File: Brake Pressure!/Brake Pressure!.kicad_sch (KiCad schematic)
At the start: 12 parts, among them J1 DTF13-6P, Q1 Q_Photo_NPN_EBC, U3 MCP2515-I, U4 TJA1050DRG, X1 ${ALTIUM_VALUE}

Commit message: Update Brake Pressure!.kicad_sch
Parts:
- renumbered C11 to C1, C12 to C2, C13 to C3, C14 to C4, C15 to C5, R13 to R3
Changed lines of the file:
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@@
 		(on_board yes)
 		(dnp no)
-		(property "Reference" "C14"
+		(property "Reference" "C4"
 			(at 96.901 144.272 0)
 			(effects
@@
 			(project "Brake Pressure!"
 				(path "/966ccee8-1e79-48cc-adf9-5a781a378016"
-					(reference "C14")
+					(reference "C4")
 					(unit 0)
 				)
@@
 		(on_board yes)
 		(dnp no)
-		(property "Reference" "C13"
+		(property "Reference" "C3"
 			(at 96.139 134.112 0)
 			(effects
@@
 			(project "Brake Pressure!"
 				(path "/966ccee8-1e79-48cc-adf9-5a781a378016"
-					(reference "C13")
+					(reference "C3")
 					(unit 0)
 				)
@@
 		(on_board yes)
 		(dnp no)
-		(property "Reference" "C11"
+		(property "Reference" "C1"
 			(at 61.722 127.762 0)
 			(effects
@@
 			(project "Brake Pressure!"
 				(path "/966ccee8-1e79-48cc-adf9-5a781a378016"
-					(reference "C11")
+					(reference "C1")
 					(unit 0)
 				)
@@
 		(on_board yes)
 		(dnp no)
-		(property "Reference" "C12"
+		(property "Reference" "C2"
 			(at 90.17 127 0)
 			(effects
@@
 			(project "Brake Pressure!"
 				(path "/966ccee8-1e79-48cc-adf9-5a781a378016"
-					(reference "C12")
+					(reference "C2")
 					(unit 0)
 				)
@@
 		(on_board yes)
 		(dnp no)
-		(property "Reference" "C15"
+		(property "Reference" "C5"
 			(at 246.38 135.89 0)
 			(effects
@@
 			(project "Brake Pressure!"
 				(path "/966ccee8-1e79-48cc-adf9-5a781a378016"
-					(reference "C15")
+					(reference "C5")
 					(unit 0)
 				)
@@
 		(dnp no)
 		(fields_autoplaced yes)
-		(property "Reference" "R13"
+		(property "Reference" "R3"
 			(at 109.22 115.57 90)
 			(effects
@@
 			(project "Brake Pressure!"
 				(path "/966ccee8-1e79-48cc-adf9-5a781a378016"
-					(reference "R13")
+					(reference "R3")
 					(unit 1)
 				)

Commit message: brake pressure
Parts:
- renumbered U4 to U1, U3 to U2
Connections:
- no-connect marks 8 -> 7
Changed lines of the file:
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@@
-	)
-	(no_connect
-		(at 156.21 129.54)
 	)
 	(no_connect
@@
 	(wire
 		(pts
+			(xy 25.4 38.1) (xy 30.48 38.1)
+		)
+		(stroke
+			(width 0)
+			(type default)
+		)
+	)
+	(wire
+		(pts
 			(xy 177.8 111.76) (xy 177.8 121.92)
 		)
@@
 	(wire
 		(pts
+			(xy 25.4 165.1) (xy 25.4 38.1)
+		)
+		(stroke
+			(width 0)
+			(type default)
+		)
+	)
+	(wire
+		(pts
 			(xy 104.14 133.35) (xy 104.14 134.62)
 		)
@@
 	(wire
 		(pts
+			(xy 163.83 165.1) (xy 25.4 165.1)
+		)
+		(stroke
+			(width 0)
+			(type default)
+		)
+	)
+	(wire
+		(pts
 			(xy 236.22 121.92) (xy 257.81 121.92)
 		)
@@
 	(wire
 		(pts
+			(xy 156.21 129.54) (xy 163.83 129.54)
+		)
+		(stroke
+			(width 0)
+			(type default)
+		)
+	)
+	(wire
+		(pts
 			(xy 43.18 81.28) (xy 43.18 85.09)
 		)
@@
 		(pts
 			(xy 93.98 113.03) (xy 93.98 121.92)
+		)
+		(stroke
+			(width 0)
+			(type default)
+		)
+	)
+	(wire
+		(pts
+			(xy 163.83 129.54) (xy 163.83 165.1)
 		)
 		(stroke
@@
 		(on_board yes)
 		(dnp no)
-		(property "Reference" "U4"
+		(property "Reference" "U1"
 			(at 214.63 116.84 0)
 			(effects
@@
 			(project "Brake Pressure!"
 				(path "/966ccee8-1e79-48cc-adf9-5a781a378016"
-					(reference "U4")
+					(reference "U1")
 					(unit 0)
 				)
@@
 		(on_board yes)
 		(dnp no)
-		(property "Reference" "U3"
+		(property "Reference" "U2"
 			(at 123.19 104.14 0)
 			(effects
@@
 			(project "Brake Pressure!"
 				(path "/966ccee8-1e79-48cc-adf9-5a781a378016"
-					(reference "U3")
+					(reference "U2")
 					(unit 0)
 				)

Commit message: make new connection
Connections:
- net CS: now also A1.13 (D10)
- net SCK: now also A1.16 (SCK)
- net SI: now also A1.14 (MOSI)
- net SO: now also A1.15 (MISO)
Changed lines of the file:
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@@
+		)
+	)
+	(global_label "SCK"
+		(shape input)
+		(at 30.48 68.58 180)
+		(fields_autoplaced yes)
+		(effects
+			(font
+				(size 1.27 1.27)
+			)
+			(justify right)
+		)
+		(property "Intersheetrefs" "${INTERSHEET_REFS}"
+			(at 23.7453 68.58 0)
+			(effects
+				(font
+					(size 1.27 1.27)
+				)
+				(justify right)
+				(hide yes)
+			)
 		)
 	)
@@
 		)
 	)
+	(global_label "CS"
+		(shape input)
+		(at 30.48 58.42 180)
+		(fields_autoplaced yes)
+		(effects
+			(font
+				(size 1.27 1.27)
+			)
+			(justify right)
+		)
+		(property "Intersheetrefs" "${INTERSHEET_REFS}"
+			(at 25.0153 58.42 0)
+			(effects
+				(font
+					(size 1.27 1.27)
+				)
+				(justify right)
+				(hide yes)
+			)
+		)
+	)
 	(global_label "Low"
 		(shape input)
@@
 		)
 	)
+	(global_label "SI"
+		(shape input)
+		(at 30.48 63.5 180)
+		(fields_autoplaced yes)
+		(effects
+			(font
+				(size 1.27 1.27)
+			)
+			(justify right)
+		)
+		(property "Intersheetrefs" "${INTERSHEET_REFS}"
+			(at 25.6805 63.5 0)
+			(effects
+				(font
+					(size 1.27 1.27)
+				)
+				(justify right)
+				(hide yes)
+			)
+		)
+	)
 	(global_label "SO"
 		(shape input)
@@
 				(hide yes)
 			)
+		)
+	)
+	(global_label "SO"
+		(shape input)
+		(at 30.48 66.04 180)
+		(fields_autoplaced yes)
+		(effects
+			(font
+				(size 1.27 1.27)
+			)
+			(justify right)
+		)
+		(property "Intersheetrefs" "${INTERSHEET_REFS}"
+			(at 24.9548 66.04 0)
+			(effects
+				(font
+					(size 1.27 1.27)
+				)
+				(justify right)
+				(hide yes)
+			)

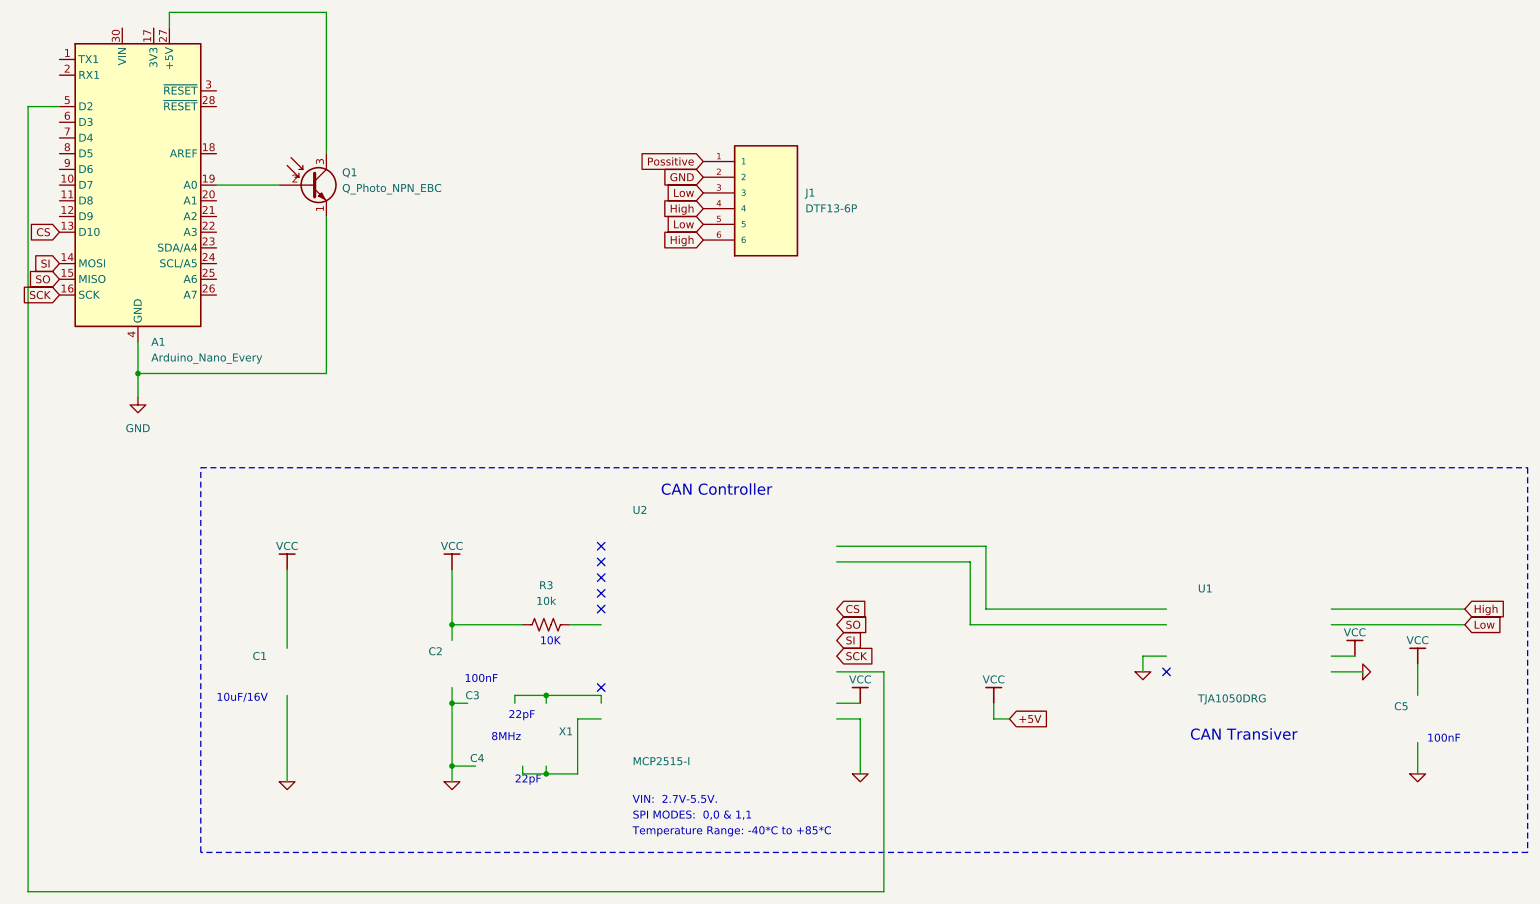
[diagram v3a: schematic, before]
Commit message: brake pressure done
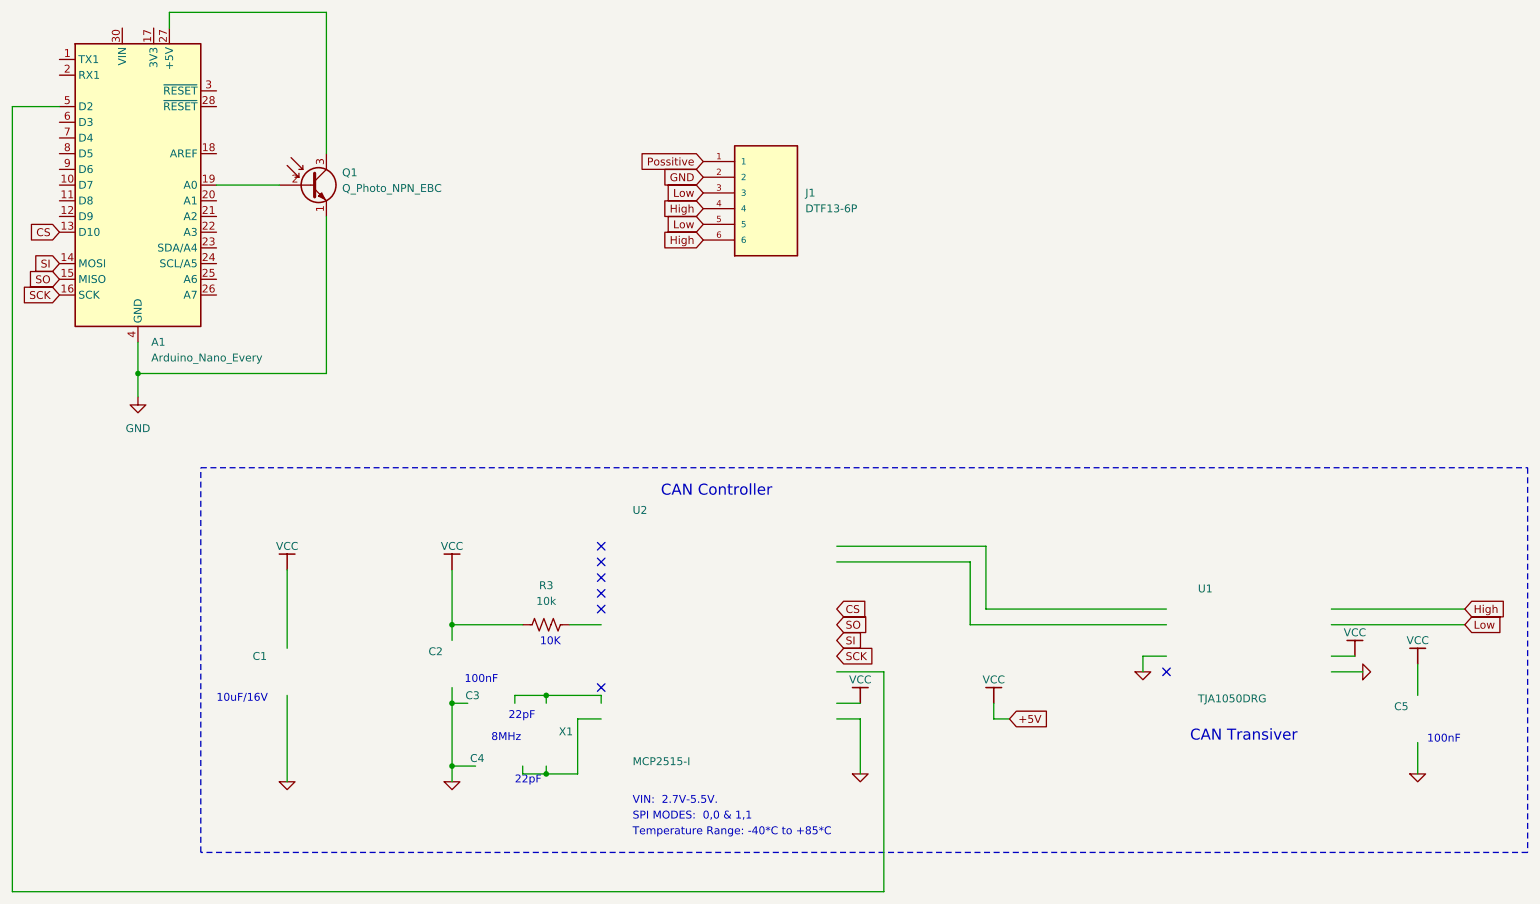
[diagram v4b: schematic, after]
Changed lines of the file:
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@@
 	(wire
 		(pts
-			(xy 25.4 38.1) (xy 30.48 38.1)
+			(xy 22.86 38.1) (xy 30.48 38.1)
 		)
 		(stroke
@@
 	(wire
 		(pts
-			(xy 25.4 165.1) (xy 25.4 38.1)
+			(xy 22.86 165.1) (xy 22.86 38.1)
 		)
 		(stroke
@@
 	(wire
 		(pts
-			(xy 163.83 165.1) (xy 25.4 165.1)
+			(xy 163.83 165.1) (xy 22.86 165.1)
 		)
 		(stroke
